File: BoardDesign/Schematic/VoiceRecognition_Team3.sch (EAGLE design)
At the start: 52 parts, among them J1 5.5x2.1mm Barrel, Q1 16MHz, X1 USB-A

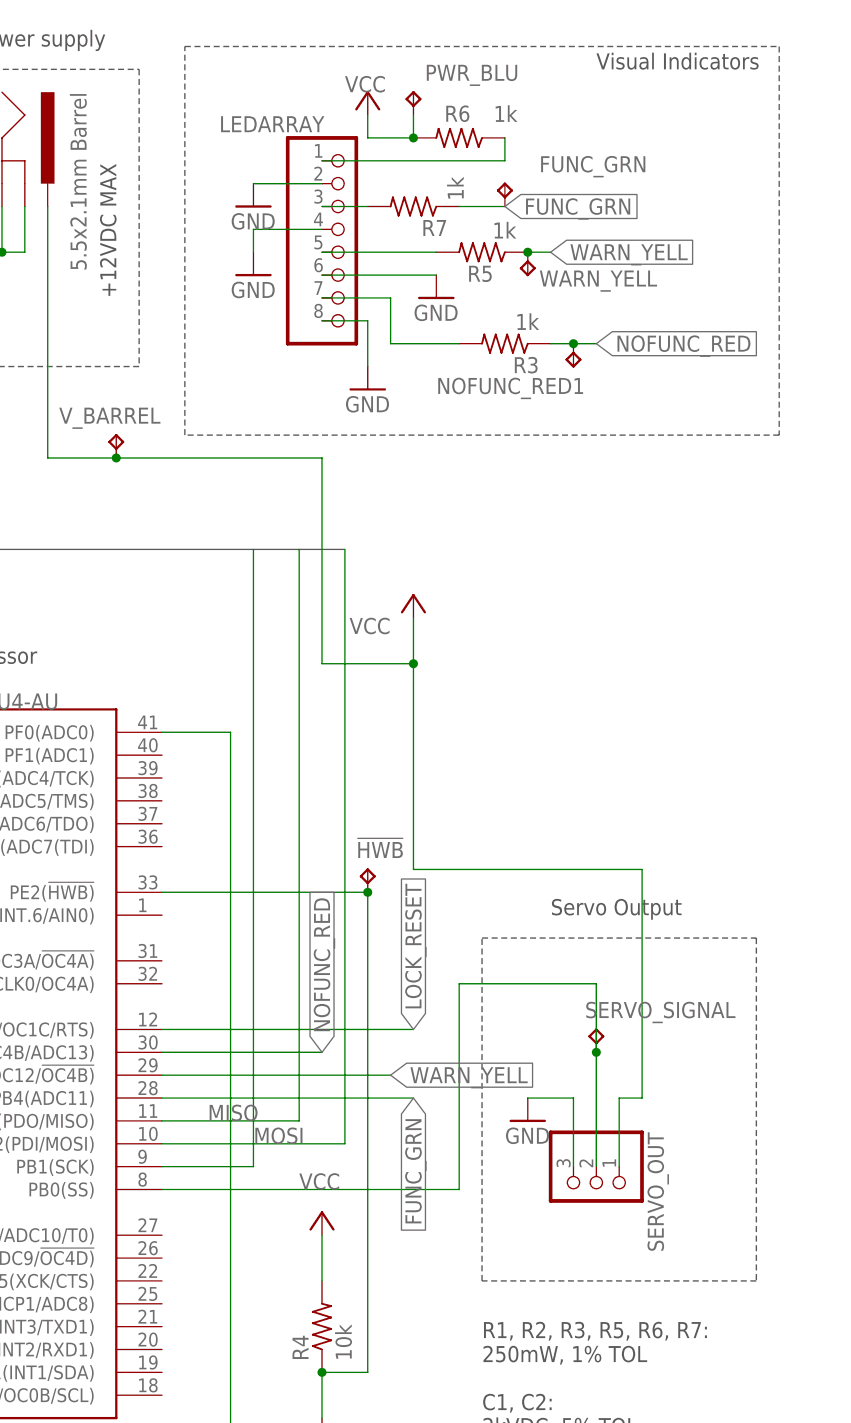
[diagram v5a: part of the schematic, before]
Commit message: Vias & Ground Plane
*Verified that all vias tied to GND were stiched. Wondering if we need additional ground stitching vias around the board?
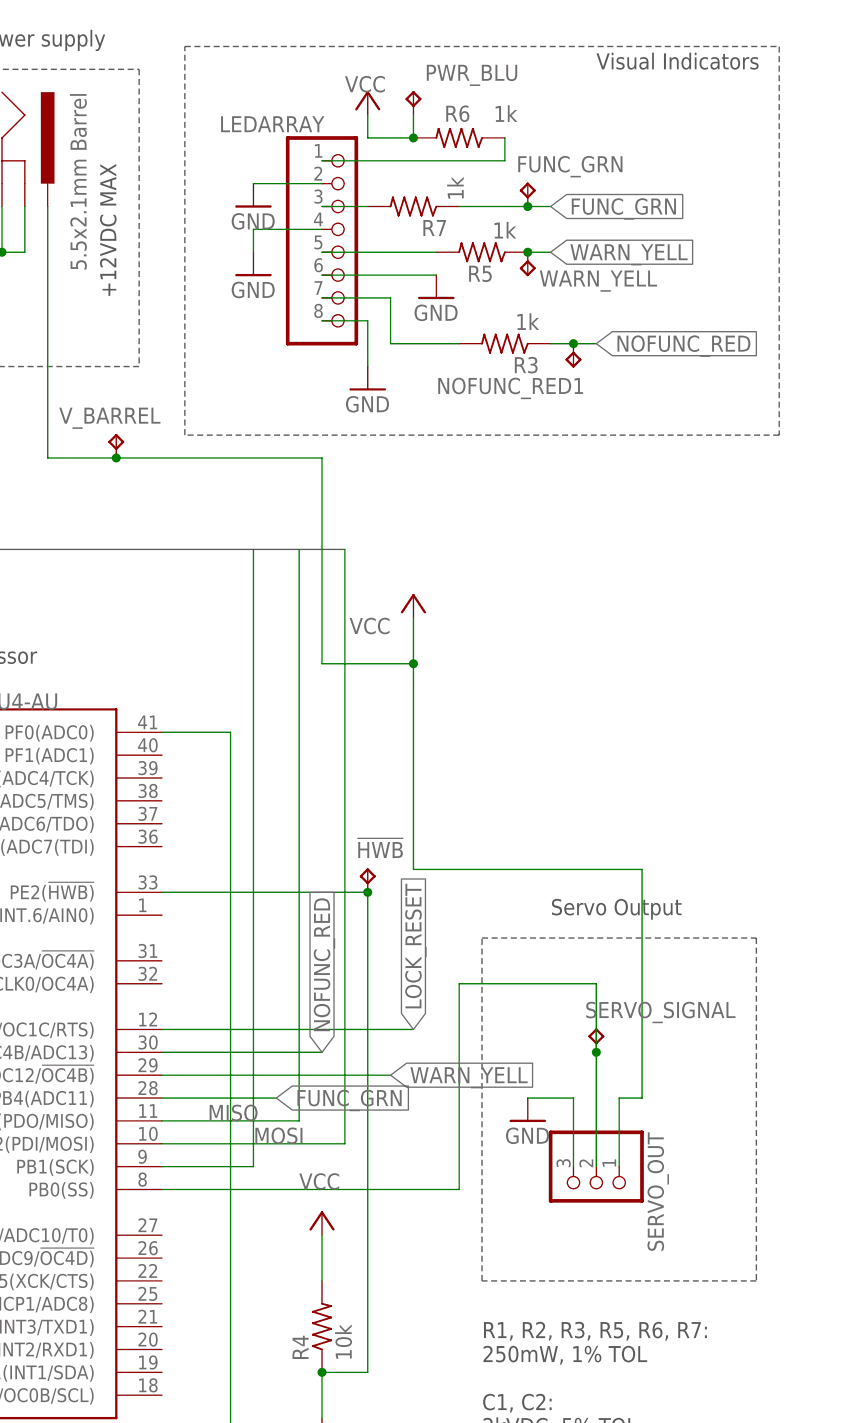
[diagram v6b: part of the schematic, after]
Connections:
- new net N$8: LEDARRAY.3, R7.2
- net FUNC_GRN: no longer LEDARRAY.3, R7.2
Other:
- moved on the sheet: FUNC_GRN
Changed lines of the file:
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@@
 <part name="GND_ICSP" library="testpad" library_urn="urn:adsk.eagle:library:385" deviceset="TP" device="TP15SQ" package3d_urn="urn:adsk.eagle:package:27975/1"/>
 <part name="PWR_BLU" library="testpad" library_urn="urn:adsk.eagle:library:385" deviceset="TP" device="TP15SQ" package3d_urn="urn:adsk.eagle:package:27975/1"/>
-<part name="FUNC_GRN" library="testpad" library_urn="urn:adsk.eagle:library:385" deviceset="TP" device="TP15SQ" package3d_urn="urn:adsk.eagle:package:27975/1"/>
 <part name="WARN_YELL" library="testpad" library_urn="urn:adsk.eagle:library:385" deviceset="TP" device="TP15SQ" package3d_urn="urn:adsk.eagle:package:27975/1"/>
 <part name="!HWB" library="testpad" library_urn="urn:adsk.eagle:library:385" deviceset="TP" device="TP15SQ" package3d_urn="urn:adsk.eagle:package:27975/1"/>
@@
 <part name="GND22" library="supply1" library_urn="urn:adsk.eagle:library:371" deviceset="GND" device=""/>
 <part name="NOFUNC_RED1" library="testpad" library_urn="urn:adsk.eagle:library:385" deviceset="TP" device="TP15SQ" package3d_urn="urn:adsk.eagle:package:27975/1"/>
+<part name="FUNC_GRN" library="testpad" library_urn="urn:adsk.eagle:library:385" deviceset="TP" device="TP15SQ" package3d_urn="urn:adsk.eagle:package:27975/1"/>
 </parts>
 <sheets>
@@
 <attribute name="TP_SIGNAL_NAME" x="234.95" y="179.07" size="1.778" layer="97"/>
 </instance>
-<instance part="FUNC_GRN" gate="G$1" x="243.84" y="170.18">
-<attribute name="NAME" x="247.65" y="171.45" size="1.778" layer="95"/>
-<attribute name="TP_SIGNAL_NAME" x="245.11" y="168.91" size="1.778" layer="97"/>
-</instance>
 <instance part="WARN_YELL" gate="G$1" x="246.38" y="160.02" rot="R180">
 <attribute name="NAME" x="247.65" y="158.75" size="1.778" layer="95"/>
@@
 <attribute name="NAME" x="252.73" y="148.59" size="1.778" layer="95" rot="R180"/>
 <attribute name="TP_SIGNAL_NAME" x="250.19" y="151.13" size="1.778" layer="97" rot="R180"/>
+</instance>
+<instance part="FUNC_GRN" gate="G$1" x="246.38" y="170.18">
+<attribute name="NAME" x="245.11" y="171.45" size="1.778" layer="95"/>
+<attribute name="TP_SIGNAL_NAME" x="247.65" y="168.91" size="1.778" layer="97"/>
 </instance>
 </instances>
@@
 <wire x1="33.02" y1="91.44" x2="33.02" y2="93.98" width="0.1524" layer="91"/>
 <junction x="33.02" y="93.98"/>
-</segment>
-</net>
-<net name="FUNC_GRN" class="0">
-<segment>
-<pinref part="LEDARRAY" gate="G$1" pin="3"/>
-<wire x1="228.6" y1="167.64" x2="223.52" y2="167.64" width="0.1524" layer="91"/>
-<pinref part="R7" gate="G$1" pin="2"/>
-</segment>
-<segment>
-<pinref part="U$1" gate="G$1" pin="PB4(ADC11)"/>
-<wire x1="205.74" y1="68.58" x2="233.68" y2="68.58" width="0.1524" layer="91"/>
-<label x="233.68" y="68.58" size="1.778" layer="95" rot="R270" xref="yes"/>
-</segment>
-<segment>
-<pinref part="FUNC_GRN" gate="G$1" pin="TP"/>
-<wire x1="243.84" y1="167.64" x2="238.76" y2="167.64" width="0.1524" layer="91"/>
-<label x="243.84" y="167.64" size="1.778" layer="95" xref="yes"/>
-<pinref part="R7" gate="G$1" pin="1"/>
 </segment>
 </net>
@@
 </segment>
 </net>
+<net name="N$8" class="0">
+<segment>
+<pinref part="LEDARRAY" gate="G$1" pin="3"/>
+<pinref part="R7" gate="G$1" pin="2"/>
+<wire x1="223.52" y1="167.64" x2="228.6" y2="167.64" width="0.1524" layer="91"/>
+</segment>
+</net>
+<net name="FUNC_GRN" class="0">
+<segment>
+<pinref part="U$1" gate="G$1" pin="PB4(ADC11)"/>
+<wire x1="205.74" y1="68.58" x2="218.44" y2="68.58" width="0.1524" layer="91"/>
+<label x="218.44" y="68.58" size="1.778" layer="95" xref="yes"/>
+<label x="248.92" y="167.64" size="1.778" layer="95" xref="yes"/>
+</segment>
+<segment>
+<pinref part="R7" gate="G$1" pin="1"/>
+<wire x1="238.76" y1="167.64" x2="246.38" y2="167.64" width="0.1524" layer="91"/>
+<pinref part="FUNC_GRN" gate="G$1" pin="TP"/>
+<wire x1="246.38" y1="167.64" x2="248.92" y2="167.64" width="0.1524" layer="91"/>
+<junction x="246.38" y="167.64"/>
+</segment>
+</net>

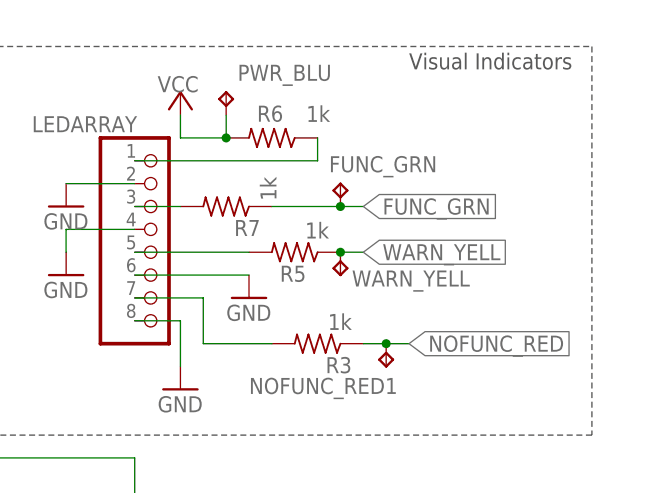
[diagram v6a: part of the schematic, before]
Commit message: Rearranges
* Moved some components around per Tom's suggestons. Edits from 11/12; forgot to push to git.,
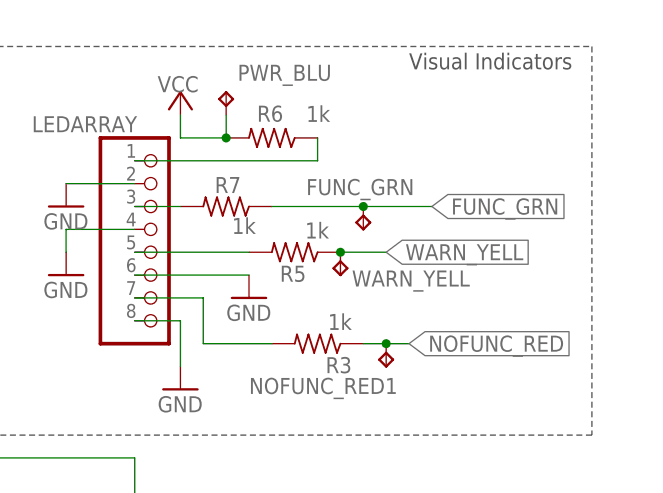
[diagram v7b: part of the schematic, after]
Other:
- moved on the sheet: FUNC_GRN
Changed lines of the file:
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@@
 </instance>
 <instance part="R7" gate="G$1" x="233.68" y="167.64" rot="R180">
-<attribute name="NAME" x="237.49" y="166.1414" size="1.778" layer="95" rot="R180"/>
-<attribute name="VALUE" x="237.49" y="170.942" size="1.778" layer="96" rot="R270"/>
+<attribute name="NAME" x="232.41" y="169.1386" size="1.778" layer="95"/>
+<attribute name="VALUE" x="236.982" y="166.37" size="1.778" layer="96" rot="R180"/>
 </instance>
 <instance part="GND2" gate="1" x="215.9" y="167.64">
@@
 <attribute name="TP_SIGNAL_NAME" x="250.19" y="151.13" size="1.778" layer="97" rot="R180"/>
 </instance>
-<instance part="FUNC_GRN" gate="G$1" x="246.38" y="170.18">
-<attribute name="NAME" x="245.11" y="171.45" size="1.778" layer="95"/>
-<attribute name="TP_SIGNAL_NAME" x="247.65" y="168.91" size="1.778" layer="97"/>
+<instance part="FUNC_GRN" gate="G$1" x="248.92" y="165.1" rot="R180">
+<attribute name="NAME" x="242.57" y="168.91" size="1.778" layer="95"/>
+<attribute name="TP_SIGNAL_NAME" x="247.65" y="166.37" size="1.778" layer="97" rot="R180"/>
 </instance>
 </instances>
@@
 <segment>
 <pinref part="R5" gate="G$1" pin="1"/>
-<wire x1="246.38" y1="162.56" x2="248.92" y2="162.56" width="0.1524" layer="91"/>
-<label x="248.92" y="162.56" size="1.778" layer="95" xref="yes"/>
+<wire x1="246.38" y1="162.56" x2="251.46" y2="162.56" width="0.1524" layer="91"/>
+<label x="251.46" y="162.56" size="1.778" layer="95" xref="yes"/>
 <pinref part="WARN_YELL" gate="G$1" pin="TP"/>
 <junction x="246.38" y="162.56"/>
@@
 <wire x1="205.74" y1="68.58" x2="218.44" y2="68.58" width="0.1524" layer="91"/>
 <label x="218.44" y="68.58" size="1.778" layer="95" xref="yes"/>
-<label x="248.92" y="167.64" size="1.778" layer="95" xref="yes"/>
 </segment>
 <segment>
 <pinref part="R7" gate="G$1" pin="1"/>
-<wire x1="238.76" y1="167.64" x2="246.38" y2="167.64" width="0.1524" layer="91"/>
+<wire x1="238.76" y1="167.64" x2="248.92" y2="167.64" width="0.1524" layer="91"/>
 <pinref part="FUNC_GRN" gate="G$1" pin="TP"/>
-<wire x1="246.38" y1="167.64" x2="248.92" y2="167.64" width="0.1524" layer="91"/>
-<junction x="246.38" y="167.64"/>
-</segment>
-</net>
+<junction x="248.92" y="167.64"/>
+<wire x1="256.54" y1="167.64" x2="248.92" y2="167.64" width="0.1524" layer="91"/>
+<label x="256.54" y="167.64" size="1.778" layer="95" xref="yes"/>
+</segment>
+</net>
